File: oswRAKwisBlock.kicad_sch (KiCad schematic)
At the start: 1 part, among them J1 WisBlock

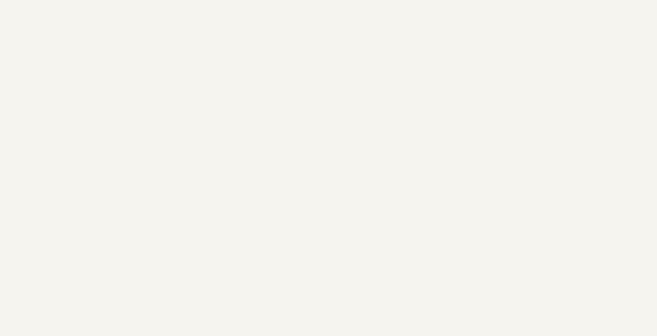
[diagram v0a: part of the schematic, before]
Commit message: Getting the wisblock footprint on the board.
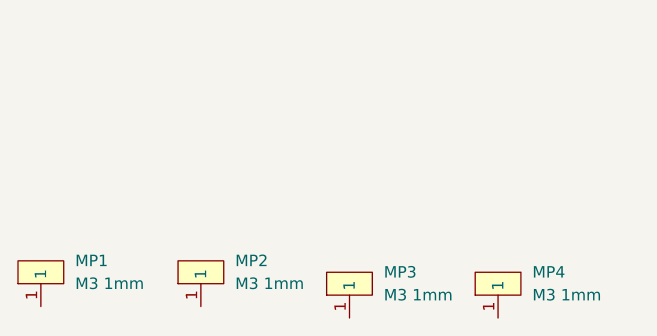
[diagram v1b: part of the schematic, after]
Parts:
- added MP1, MP2, MP3, MP4: M3 1mm, AllardMountingHW:MTGNP300H213Z565, symbol AllardMountingHW:MP_genericHole

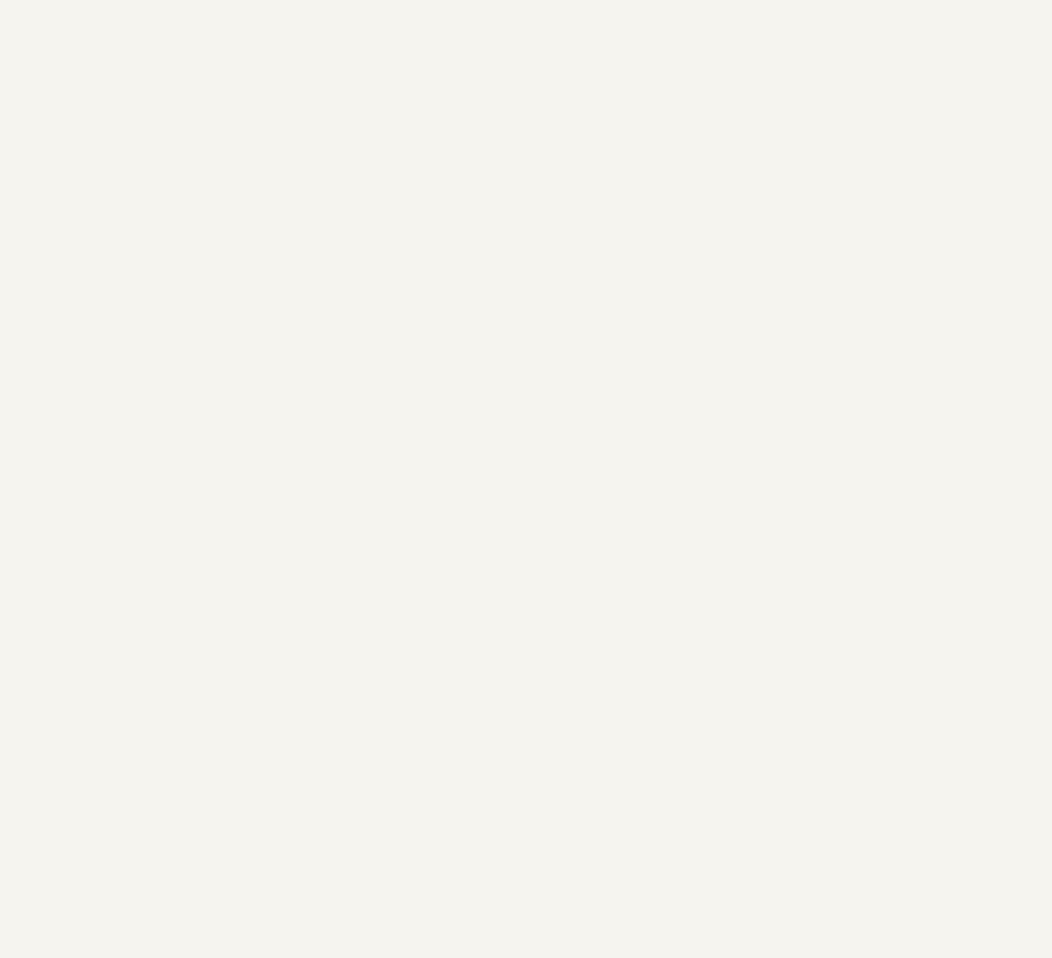
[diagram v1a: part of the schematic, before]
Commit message: Fixing the mounting hole issue.
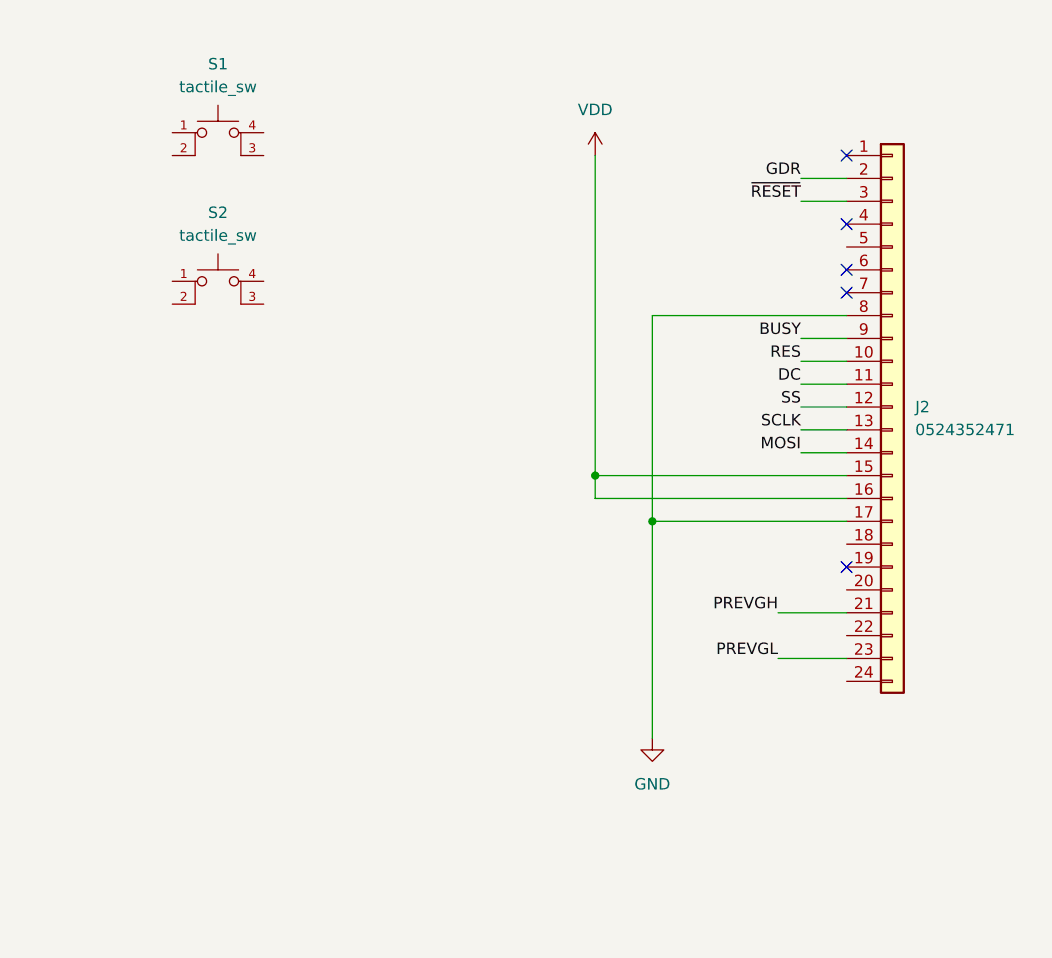
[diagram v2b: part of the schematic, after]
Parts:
- added J2: 0524352471, AllardConnFootPrints:MOLEX_52435-2471, symbol AllardConn:J10027
- added S1, S2: tactile_sw, AllardSpecialFootPrints:Panasonic_EVQPUA02K, symbol AllardSwitch:S10002
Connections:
- new net BUSY: J2.9 (Pin_9)
- new net DC: J2.11 (Pin_11)
- new net GDR: J2.2 (Pin_2)
- new net GND: J2.17 (Pin_17), J2.8 (Pin_8)
- new net MOSI: J2.14 (Pin_14)
- new net PREVGH: J2.21 (Pin_21)
- new net PREVGL: J2.23 (Pin_23)
- new net RES: J2.10 (Pin_10)
- new net SCLK: J2.13 (Pin_13)
- new net SS: J2.12 (Pin_12)
- new net VDD: J2.15 (Pin_15), J2.16 (Pin_16)
- new net ~{RESET}: J2.3 (Pin_3)
- no-connect marks 0 -> 5

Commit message: Updates.
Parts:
- added R1, R2, R3: 10k, AllardChip:RESC40X20X15L10N, symbol AllardPassive:R10020-10000
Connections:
- net GND: now also J1.39 (FS3), J1.40 (GND), J1.FS1 (GND), J1.FS2 (GND), J1.FS4 (GND), S1.3 (K), S1.4 (A), S2.3 (K), S2.4 (A)
- net VDD: now also J1.5 (3V3), R1.1, R2.1, R3.1
- net at J1.13 (RESET): now also R3.2
- net at S2.1: now also S2.2, R2.2
- net at S1.1: now also S1.2, R1.2

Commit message: Working forward.
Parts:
- added Q1: SI1308EDL-T1-GE3, AllardSOT:SOT23-3P65_210X110L20X32N, symbol AllardSemicon:Q10007
- added U1: MCP73811T-420I/OT, AllardSOT:SOT23-5P95_270X145L35X35N, symbol AllardPower:U40004

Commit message: Updates.
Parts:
- added C1, C2, C3, C4, C5, C6, C7: 1u, AllardChip:CAPC100X50X60L25N, symbol AllardPassive:C10A72-10001
- added J3: USB_B_Micro, AllardConnFootPrints:MOLEX_1051330011, symbol AllardConn:J10031
- added R4: 100k, AllardChip:RESC40X20X15L10N, symbol AllardPassive:R10030-10000
- added R5: 10k, AllardChip:RESC40X20X15L10N, symbol AllardPassive:R10020-10000
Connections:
- net ~{RESET} is gone; now on net GND: J2.3 (Pin_3)
- net GDR: now also Q1.1 (G), R5.1
- net GND: now also Q1.2 (S), C1.2, C2.2, C3.2, C4.2, C5.2, C6.2, C7.2, J3.5 (GND), R5.2
- net PREVGH: now also C7.1
- net RES: now also R4.2
- net VDD: now also C5.1, R4.1
- net USB_+: now reaches J1.7 (USB+)
- net USB_+: now also J3.3 (D+)
- net USB_-: now reaches J1.8 (USB-)
- net USB_-: now also J3.2 (D-)
- net at J2.18 (Pin_18): now also C4.1
- net at J2.20 (Pin_20): now also C3.1
- net at J2.22 (Pin_22): now also C2.1
- net at J2.24 (Pin_24): now also C1.1
- net at J2.5 (Pin_5): now also C6.1
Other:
- moved on the sheet: Q1, R1, R2, S1, S2

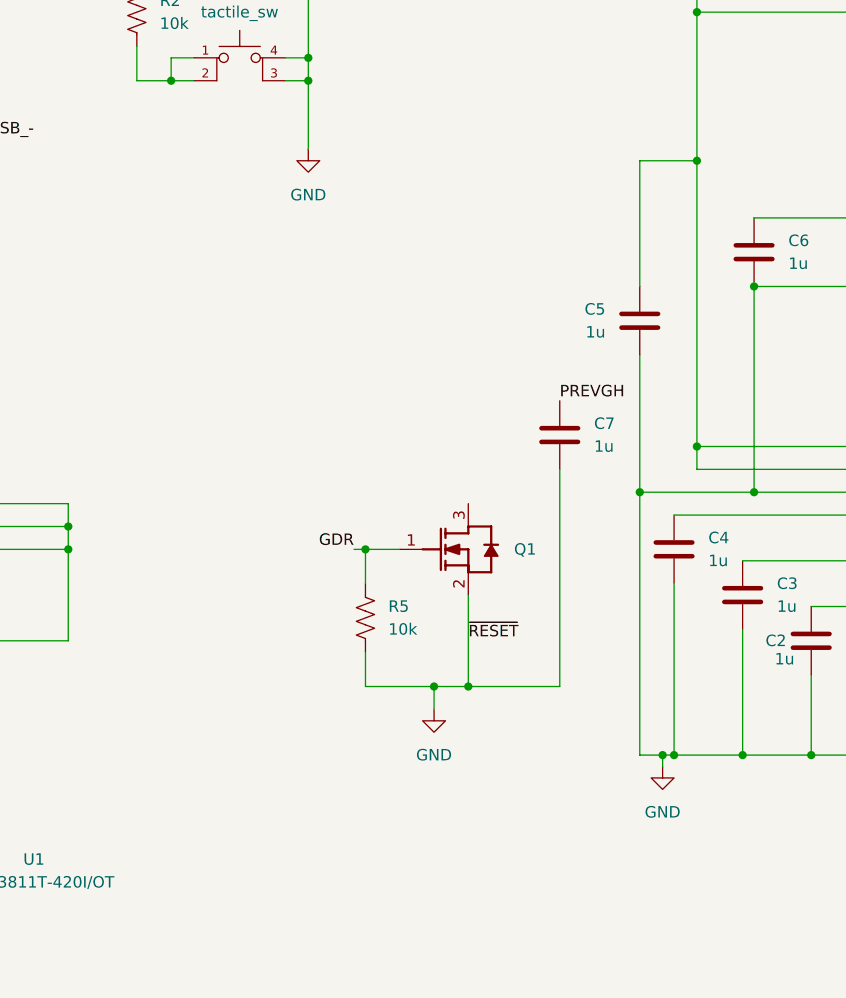
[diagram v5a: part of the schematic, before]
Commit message: Updating the board and moving some things around.
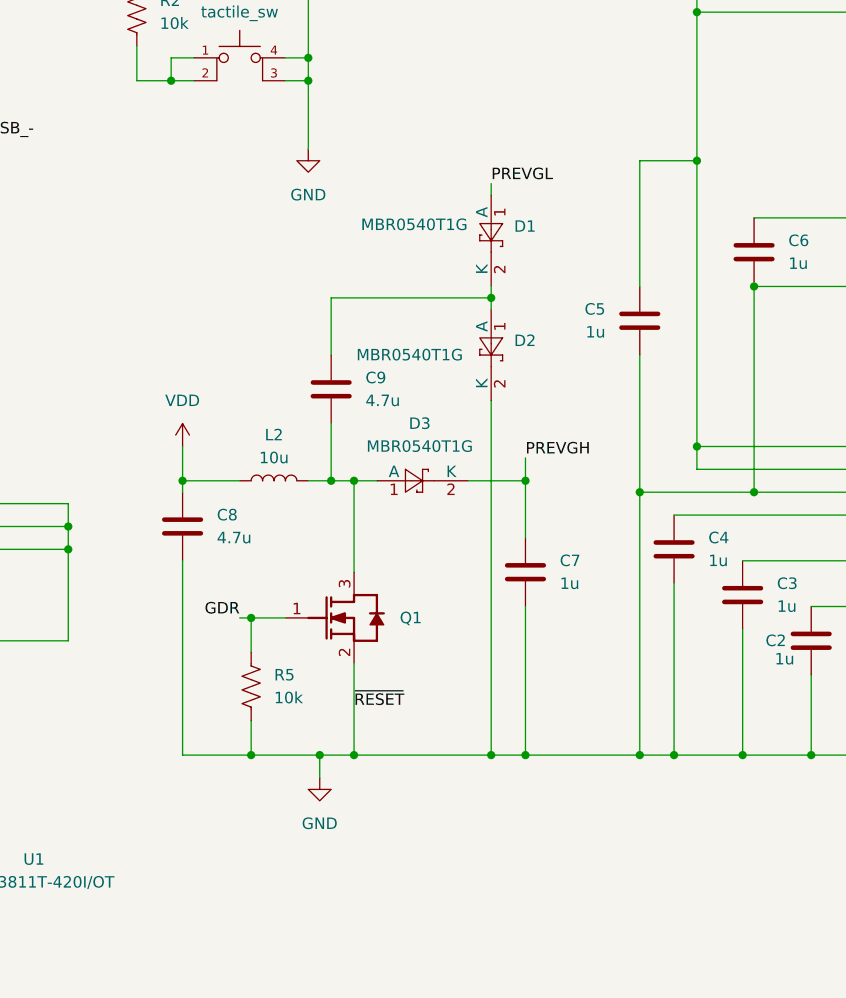
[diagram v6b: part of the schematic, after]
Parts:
- added C8, C9: 4.7u, AllardChip:CAPC200X125X145L45L, symbol AllardPassive:C47A74-10000
- added D1, D2, D3: MBR0540T1G, AllardSOD:SOD370X155X135L32X57L, symbol AllardSemicon:D10010
- added L2: 10u, AllardChip:INDC400X400X120L120L, symbol AllardPassive:L10A6X-10001
- C1, C2, C3, C4, C5, C6, C7: footprint AllardChip:CAPC100X50X60L25N -> AllardChip:CAPC100X50X60L25L
- Q1: footprint AllardSOT:SOT23-3P65_210X110L20X32N -> AllardSOT:SOT23-3P65_210X110L20X32L
- R1, R2, R3, R4, R5: footprint AllardChip:RESC40X20X15L10N -> AllardChip:RESC40X20X15L10L
- U1: footprint AllardSOT:SOT23-5P95_270X145L35X35N -> AllardSOT:SOT23-5P95_270X145L35X35L
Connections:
- net GND: now also C8.2, D2.2 (K)
- net PREVGH: now also D3.2 (K)
- net PREVGL: now also D1.1 (A)
- net VDD: now also C8.1, L2.1
- net at Q1.3 (D): now also C9.2, D3.1 (A), L2.2
- new net: C9.1, D1.2 (K), D2.1 (A)
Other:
- moved on the sheet: C7, Q1, R5

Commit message: Working on it....
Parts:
- added C10, C11: 1u, AllardChip:CAPC100X50X60L25L, symbol AllardPassive:C10A72-10000
- D1, D2, D3: footprint AllardSOD:SOD370X155X135L32X57L -> AllardSOD:SOD370X155X135L32X57N
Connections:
- net GND: now also D2.C (K), S1.2, S2.2, U1.2 (V_{SS}), C10.2, C11.2; no longer D2.2 (K), S1.3 (K), S2.3 (K)
- net PREVGH: now also D3.C (K); no longer D3.2 (K)
- net PREVGL: now also D1.A; no longer D1.1 (A)
- net at R1.2, S1.1: now also S1.3 (K); no longer S1.2
- net at C9.2, L2.2, Q1.3 (D): now also D3.A; no longer D3.1 (A)
- net at R2.2, S2.1: now also S2.3 (K); no longer S2.2
- net VUSB_BUS: now reaches U1.1 (CE)
- net VUSB_BUS: now also J3.1 (VBUS), U1.4 (V_{DD}), U1.5 (PROG), C10.1
- net at U1.3 (V_{BAT}): now also C11.1
- new net: C9.1, D1.C (K), D2.A

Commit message: Working on getting the placement settled.  VERY TIGHTgit pull!
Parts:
- added J4: 10114830-10102LF, AllardConnFootPrints:AMPHENOL_10114830-10102LF, symbol AllardConn:J10032
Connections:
- net GND: now also J4.2
- net at C11.1, U1.3 (V_{BAT}): now also J4.1
